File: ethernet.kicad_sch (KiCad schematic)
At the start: 39 parts, among them IC1 ACPL-217-500E, J6 5-2337992-8, Q17 PJE138K, U22 TPS2372-3RGWR, U23 ULS-12{slash}5-D48N-C

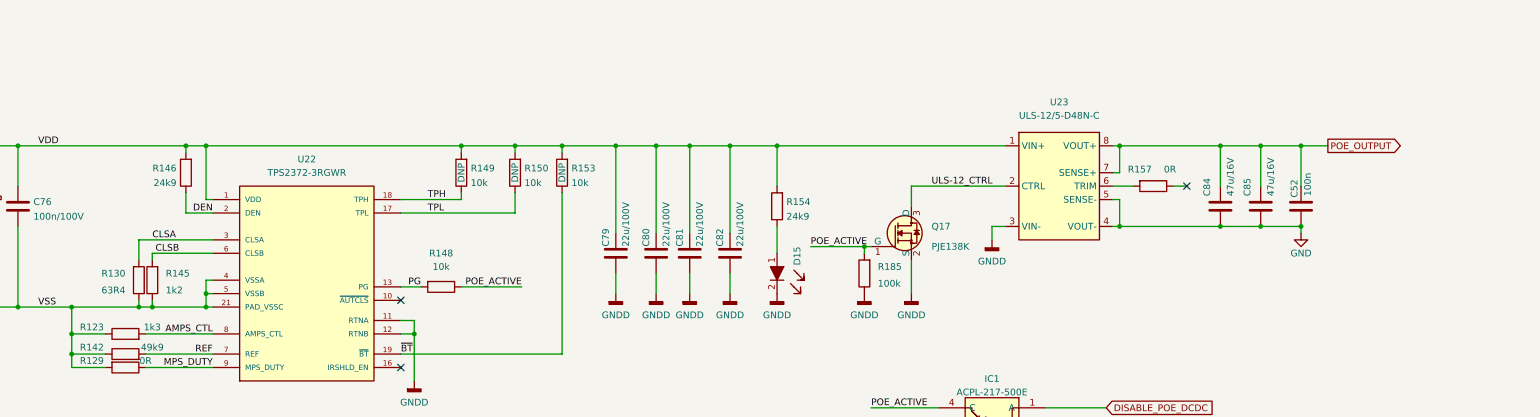
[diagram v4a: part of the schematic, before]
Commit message: Improve SMPS control circuit
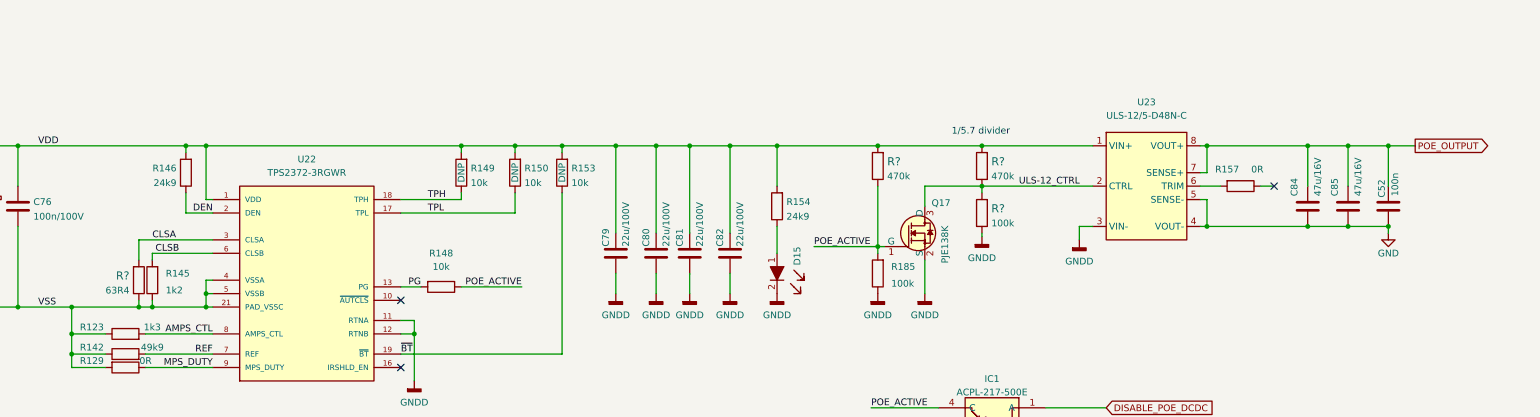
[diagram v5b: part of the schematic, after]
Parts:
- removed R130: R_63R4_0402, jetson-orin-baseboard-footprints:0402-res, symbol jetson-orin-baseboard:R_63R4_0402
- added R?: R_63R4_0603, antmicro-footprints:0603-res, symbol antmicroResistors0603:R_63R4_0603
- added R? (x2): R_470k_0402, antmicro-footprints:0402-res, symbol antmicroResistors0402:R_470k_0402
- added R?: R_100k_0402, antmicro-footprints:0402-res, symbol antmicroResistors0402:R_100k_0402
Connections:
- net CLSA: now also R?.2
- net GNDD: now also R?.1
- net POE_ACTIVE: now also R?.1
- net ULS-12_CTRL: now also R?.1, R?.2
- net VDD: now also R?.2, R?.2
- net VSS: now also R?.1
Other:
- note added: "1/5.7 divider"
- moved on the sheet: C52, C84, C85, Q17, R157, R185, U23

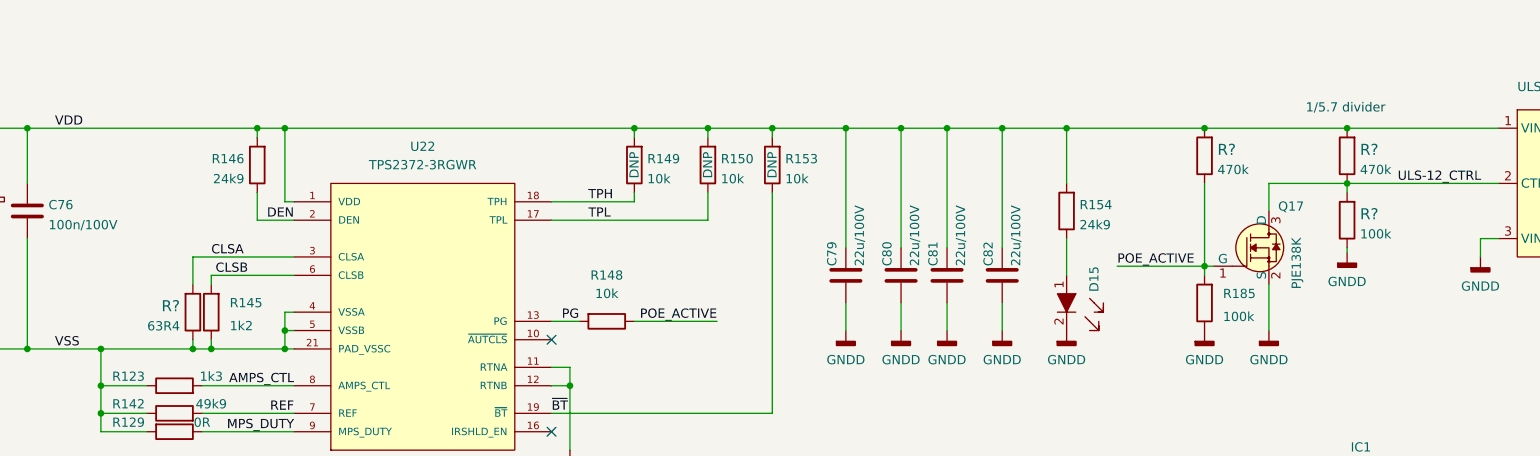
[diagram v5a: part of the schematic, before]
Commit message: Annotate parts, import them on PCB
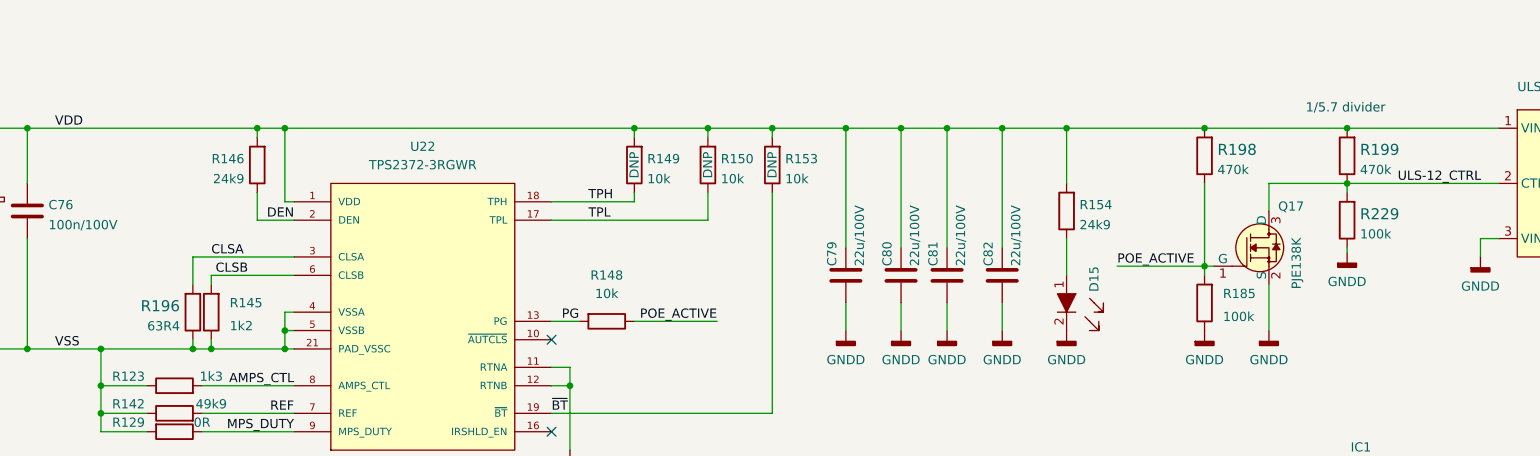
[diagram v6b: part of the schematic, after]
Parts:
- gave numbers to parts that had none: 4
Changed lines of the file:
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@@
   (symbol (lib_id "jetson-orin-baseboard:GNDD") (at 304.165 198.755 0) (unit 1)
     (in_bom yes) (on_board yes) (fields_autoplaced)
-    (property "Reference" "#PWR?" (id 0) (at 304.165 205.105 0)
+    (property "Reference" "#PWR0332" (id 0) (at 304.165 205.105 0)
       (effects (font (size 1.27 1.27)) hide)
     )
@@
   (symbol (lib_id "antmicroResistors0603:R_63R4_0603") (at 144.78 207.01 270) (mirror x) (unit 1)
     (in_bom yes) (on_board yes) (fields_autoplaced)
-    (property "Reference" "R?" (id 0) (at 143.002 206.1754 90)
+    (property "Reference" "R196" (id 0) (at 143.002 206.1754 90)
       (effects (font (size 1.524 1.524)) (justify right))
     )
@@
   (symbol (lib_id "antmicroResistors0402:R_470k_0402") (at 284.48 185.42 90) (unit 1)
     (in_bom yes) (on_board yes) (fields_autoplaced)
-    (property "Reference" "R?" (id 0) (at 286.258 184.5854 90)
+    (property "Reference" "R198" (id 0) (at 286.258 184.5854 90)
       (effects (font (size 1.524 1.524)) (justify right))
     )
@@
   (symbol (lib_id "antmicroResistors0402:R_470k_0402") (at 304.165 185.42 90) (unit 1)
     (in_bom yes) (on_board yes) (fields_autoplaced)
-    (property "Reference" "R?" (id 0) (at 305.943 184.5854 90)
+    (property "Reference" "R199" (id 0) (at 305.943 184.5854 90)
       (effects (font (size 1.524 1.524)) (justify right))
     )
@@
   (symbol (lib_id "antmicroResistors0402:R_100k_0402") (at 304.165 194.31 90) (unit 1)
     (in_bom yes) (on_board yes) (fields_autoplaced)
-    (property "Reference" "R?" (id 0) (at 305.943 193.4754 90)
+    (property "Reference" "R229" (id 0) (at 305.943 193.4754 90)
       (effects (font (size 1.524 1.524)) (justify right))
     )

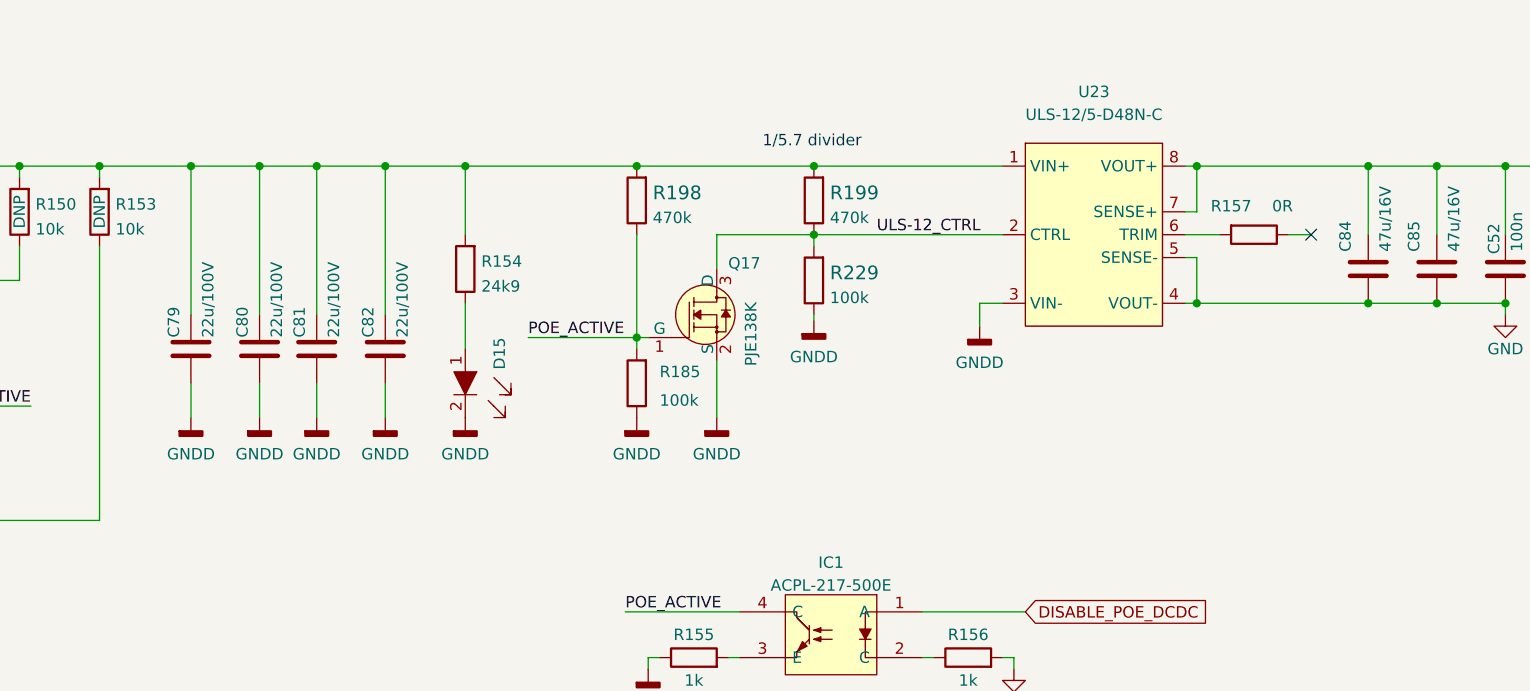
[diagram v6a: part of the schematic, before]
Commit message: Update PoE DCDC trimming resistors. Add 0R to bypass transistor on POE_ACTIVE
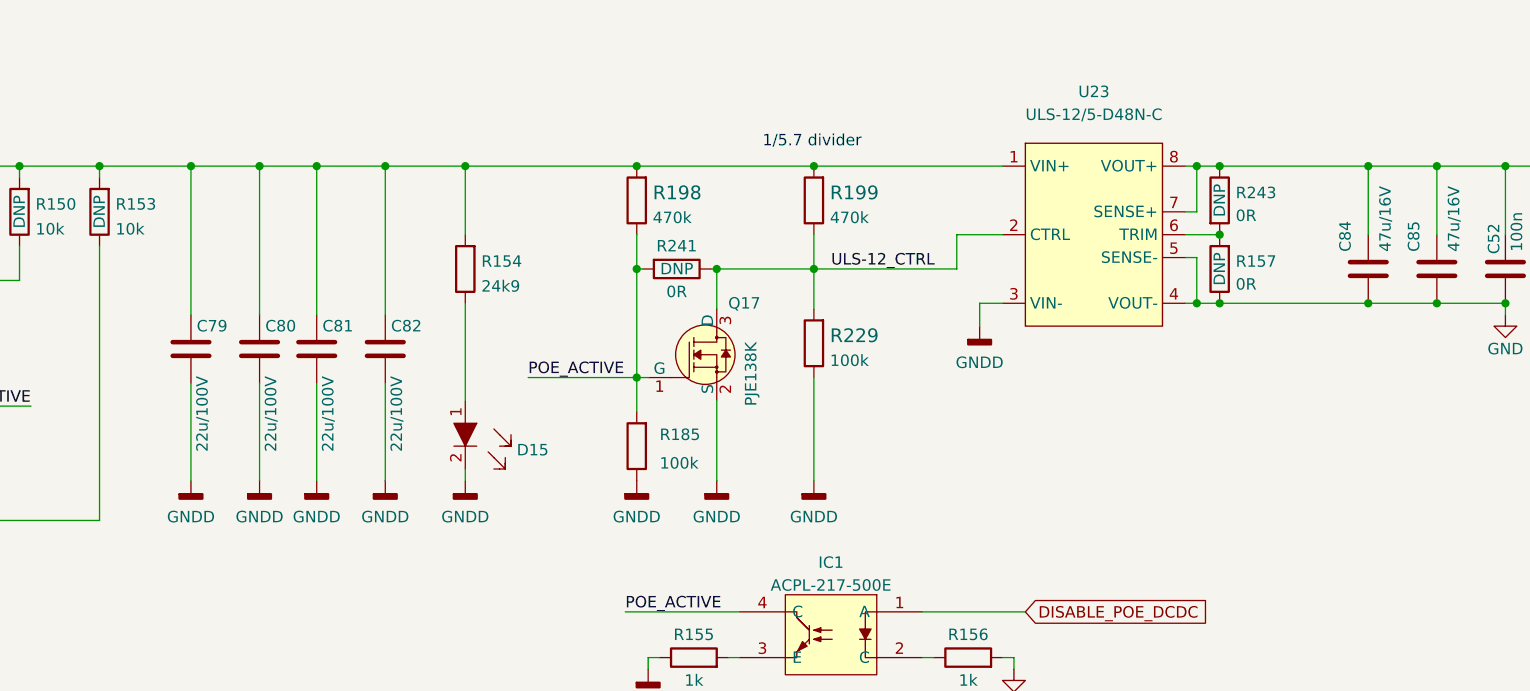
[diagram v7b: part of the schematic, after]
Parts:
- added R241: R_0R_0402, jetson-orin-baseboard-footprints:0402-res, symbol jetson-orin-baseboard:R_0R_0402
- added R243: R_0R_0603, jetson-orin-baseboard-footprints:0603-res, symbol jetson-orin-baseboard:R_0R_0603
- R157: DNP (none) -> DNP
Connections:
- net GND: now also R157.1
- net POE_ACTIVE: now also R241.2
- net POE_OUTPUT: now also R243.1
- net ULS-12_CTRL: now also R241.1
- net at R157.2, U23.6 (TRIM): now also R243.2
- no-connect marks 3 -> 2
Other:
- moved on the sheet: D15, Q17, R157, R185, R229

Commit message: Loclib
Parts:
- Q17: footprint antmicro-footprints:SOT-523 -> jetson-orin-baseboard-footprints:SOT-523; symbol antmicroTransistorsFETsMOSFETsSingle:PJE138K -> jetson-orin-baseboard:PJE138K
- R155, R156: footprint antmicro-footprints:0402-res -> jetson-orin-baseboard-footprints:0402-res; symbol antmicroResistors0402:R_1k_0402 -> jetson-orin-baseboard:R_1k_0402
- R185, R229: footprint antmicro-footprints:0402-res -> jetson-orin-baseboard-footprints:0402-res; symbol antmicroResistors0402:R_100k_0402 -> jetson-orin-baseboard:R_100k_0402
- R196: footprint antmicro-footprints:0603-res -> jetson-orin-baseboard-footprints:0603-res; symbol antmicroResistors0603:R_63R4_0603 -> jetson-orin-baseboard:R_63R4_0603
- R198, R199: footprint antmicro-footprints:0402-res -> jetson-orin-baseboard-footprints:0402-res; symbol antmicroResistors0402:R_470k_0402 -> jetson-orin-baseboard:R_470k_0402
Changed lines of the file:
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@@
     )
   )
-  (symbol (lib_id "antmicroTransistorsFETsMOSFETsSingle:PJE138K") (at 293.37 202.565 0) (unit 1)
+  (symbol (lib_id "jetson-orin-baseboard:PJE138K") (at 293.37 202.565 0) (unit 1)
     (in_bom yes) (on_board yes)
     (property "Reference" "Q17" (id 0) (at 294.64 196.85 0)
@@
       (effects (font (size 1.27 1.27)) (justify left))
     )
-    (property "Footprint" "antmicro-footprints:SOT-523" (id 2) (at 298.45 197.485 0)
+    (property "Footprint" "jetson-orin-baseboard-footprints:SOT-523" (id 2) (at 298.45 197.485 0)
       (effects (font (size 1.524 1.524)) (justify left) hide)
     )
@@
     (pin "2")
   )
-  (symbol (lib_id "antmicroResistors0402:R_1k_0402") (at 290.83 236.22 0) (unit 1)
+  (symbol (lib_id "jetson-orin-baseboard:R_1k_0402") (at 290.83 236.22 0) (unit 1)
     (in_bom yes) (on_board yes)
     (property "Reference" "R155" (id 0) (at 290.83 233.68 0))
@@
       (effects (font (size 1.27 1.27)) hide)
     )
-    (property "Footprint" "antmicro-footprints:0402-res" (id 2) (at 295.91 231.14 0)
+    (property "Footprint" "jetson-orin-baseboard-footprints:0402-res" (id 2) (at 295.91 231.14 0)
       (effects (font (size 1.524 1.524)) (justify left) hide)
     )
@@
     (pin "1")
   )
-  (symbol (lib_id "antmicroResistors0402:R_1k_0402") (at 321.31 236.22 0) (unit 1)
+  (symbol (lib_id "jetson-orin-baseboard:R_1k_0402") (at 321.31 236.22 0) (unit 1)
     (in_bom yes) (on_board yes)
     (property "Reference" "R156" (id 0) (at 321.31 233.68 0))
@@
       (effects (font (size 1.27 1.27)) hide)
     )
-    (property "Footprint" "antmicro-footprints:0402-res" (id 2) (at 326.39 231.14 0)
+    (property "Footprint" "jetson-orin-baseboard-footprints:0402-res" (id 2) (at 326.39 231.14 0)
       (effects (font (size 1.524 1.524)) (justify left) hide)
     )
@@
     (pin "2")
   )
-  (symbol (lib_name "BLM21PG221SN1D_1") (lib_id "jetson-orin-baseboard:BLM21PG221SN1D") (at 101.6 212.09 0) (unit 1)
+  (symbol (lib_id "jetson-orin-baseboard:BLM21PG221SN1D") (at 101.6 212.09 0) (unit 1)
     (in_bom yes) (on_board yes) (fields_autoplaced)
     (property "Reference" "FB3" (id 0) (at 101.6 205.74 0))
@@
     (pin "2")
   )
-  (symbol (lib_id "antmicroResistors0603:R_63R4_0603") (at 144.78 207.01 270) (mirror x) (unit 1)
+  (symbol (lib_id "jetson-orin-baseboard:R_63R4_0603") (at 144.78 207.01 270) (mirror x) (unit 1)
     (in_bom yes) (on_board yes) (fields_autoplaced)
     (property "Reference" "R196" (id 0) (at 143.002 206.1754 90)
@@
       (effects (font (size 1.524 1.524)) hide)
     )
-    (property "Footprint" "antmicro-footprints:0603-res" (id 2) (at 149.86 201.93 0)
+    (property "Footprint" "jetson-orin-baseboard-footprints:0603-res" (id 2) (at 149.86 201.93 0)
       (effects (font (size 1.524 1.524)) (justify left) hide)
     )
@@
     (pin "2")
   )
-  (symbol (lib_id "antmicroResistors0402:R_470k_0402") (at 284.48 185.42 90) (unit 1)
+  (symbol (lib_id "jetson-orin-baseboard:R_470k_0402") (at 284.48 185.42 90) (unit 1)
     (in_bom yes) (on_board yes) (fields_autoplaced)
     (property "Reference" "R198" (id 0) (at 286.258 184.5854 90)
@@
       (effects (font (size 1.524 1.524)) hide)
     )
-    (property "Footprint" "antmicro-footprints:0402-res" (id 2) (at 279.4 180.34 0)
+    (property "Footprint" "jetson-orin-baseboard-footprints:0402-res" (id 2) (at 279.4 180.34 0)
       (effects (font (size 1.524 1.524)) (justify left) hide)
     )
@@
     (pin "2")
   )
-  (symbol (lib_id "antmicroResistors0402:R_470k_0402") (at 304.165 185.42 90) (unit 1)
+  (symbol (lib_id "jetson-orin-baseboard:R_470k_0402") (at 304.165 185.42 90) (unit 1)
     (in_bom yes) (on_board yes) (fields_autoplaced)
     (property "Reference" "R199" (id 0) (at 305.943 184.5854 90)
@@
       (effects (font (size 1.524 1.524)) hide)
     )
-    (property "Footprint" "antmicro-footprints:0402-res" (id 2) (at 299.085 180.34 0)
+    (property "Footprint" "jetson-orin-baseboard-footprints:0402-res" (id 2) (at 299.085 180.34 0)
       (effects (font (size 1.524 1.524)) (justify left) hide)
     )
@@
     (pin "2")
   )
-  (symbol (lib_id "antmicroResistors0402:R_100k_0402") (at 304.165 201.295 90) (unit 1)
+  (symbol (lib_id "jetson-orin-baseboard:R_100k_0402") (at 304.165 201.295 90) (unit 1)
     (in_bom yes) (on_board yes) (fields_autoplaced)
     (property "Reference" "R229" (id 0) (at 305.943 200.4604 90)
@@
       (effects (font (size 1.524 1.524)) hide)
     )
-    (property "Footprint" "antmicro-footprints:0402-res" (id 2) (at 299.085 196.215 0)
+    (property "Footprint" "jetson-orin-baseboard-footprints:0402-res" (id 2) (at 299.085 196.215 0)
       (effects (font (size 1.524 1.524)) (justify left) hide)
     )
@@
     (pin "2")
   )
-  (symbol (lib_id "antmicroResistors0402:R_100k_0402") (at 284.48 212.725 90) (unit 1)
+  (symbol (lib_id "jetson-orin-baseboard:R_100k_0402") (at 284.48 212.725 90) (unit 1)
     (in_bom yes) (on_board yes) (fields_autoplaced)
     (property "Reference" "R185" (id 0) (at 287.02 211.455 90)
@@
       (effects (font (size 1.27 1.27)) hide)
     )
-    (property "Footprint" "antmicro-footprints:0402-res" (id 2) (at 279.4 207.645 0)
-      (effects (font (size 1.524 1.524)) (justify left) hide)
-    )
+    (property "Footprint" "jetson-orin-baseboard-footprints:0402-res" (id 2) (at 279.4 207.645 0)
+      (effects (font (size 1.524 1.524)) (justify left) hide)
+    )
